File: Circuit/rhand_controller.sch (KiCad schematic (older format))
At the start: 17 parts, among them P7 BLUETOOTH, SW1 EmSW, SW2 SWITCH_INV, U1 STM32F042, U2 IM315TRX

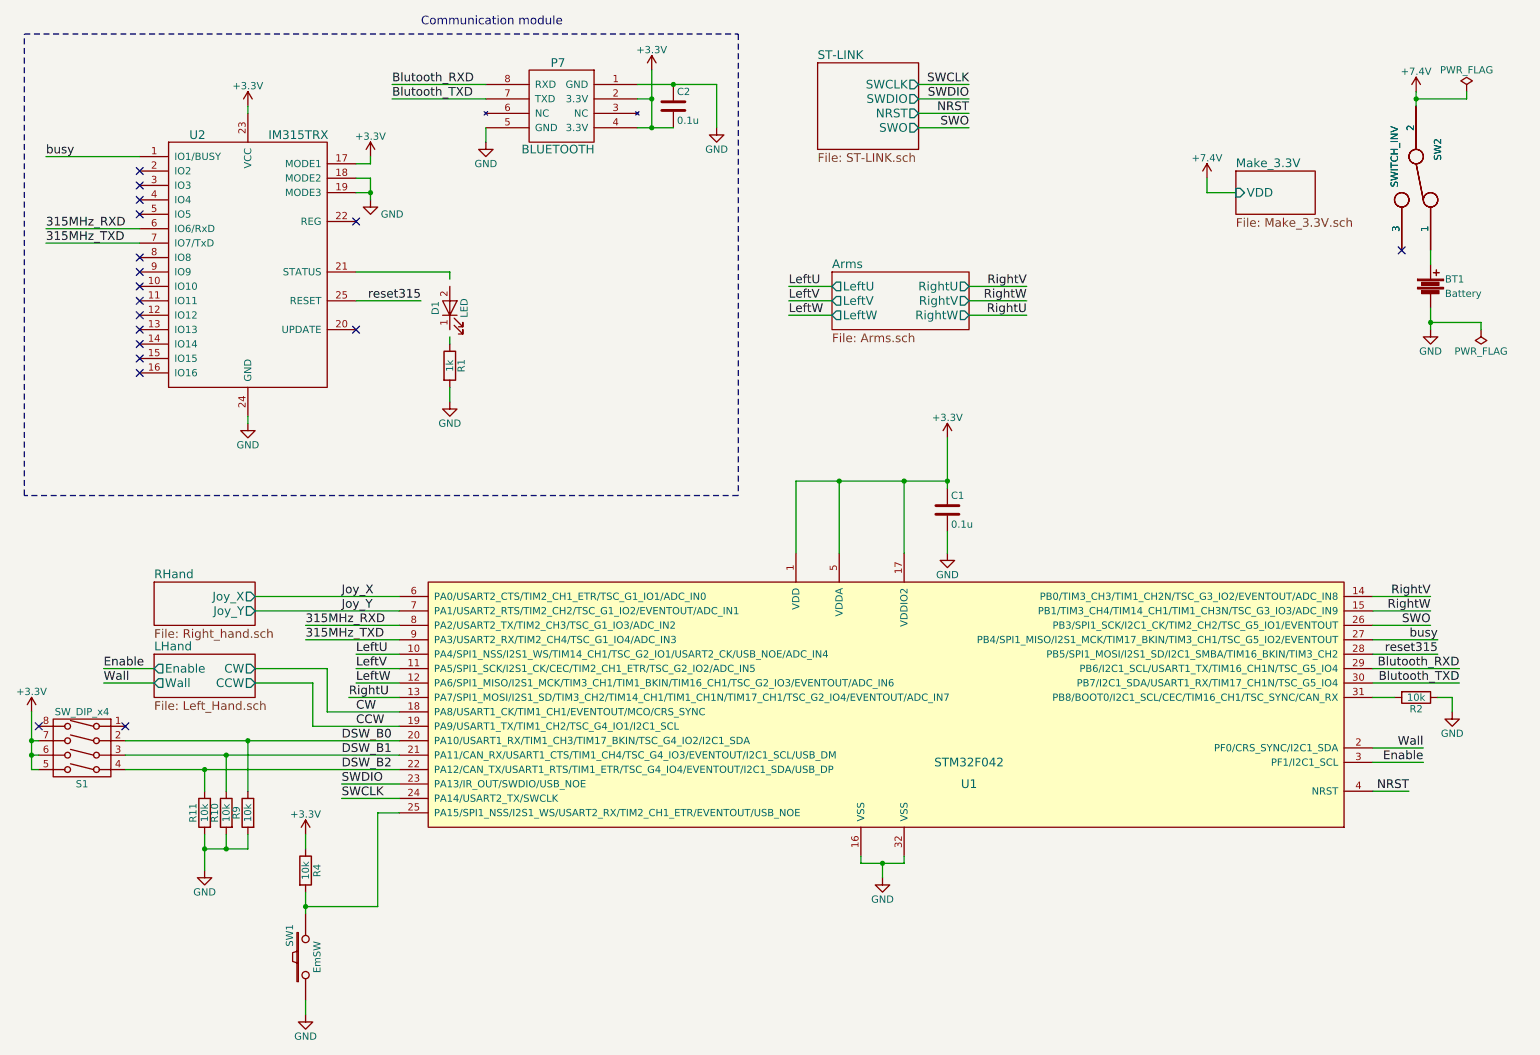
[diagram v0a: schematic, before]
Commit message: 部品割り付けの完了
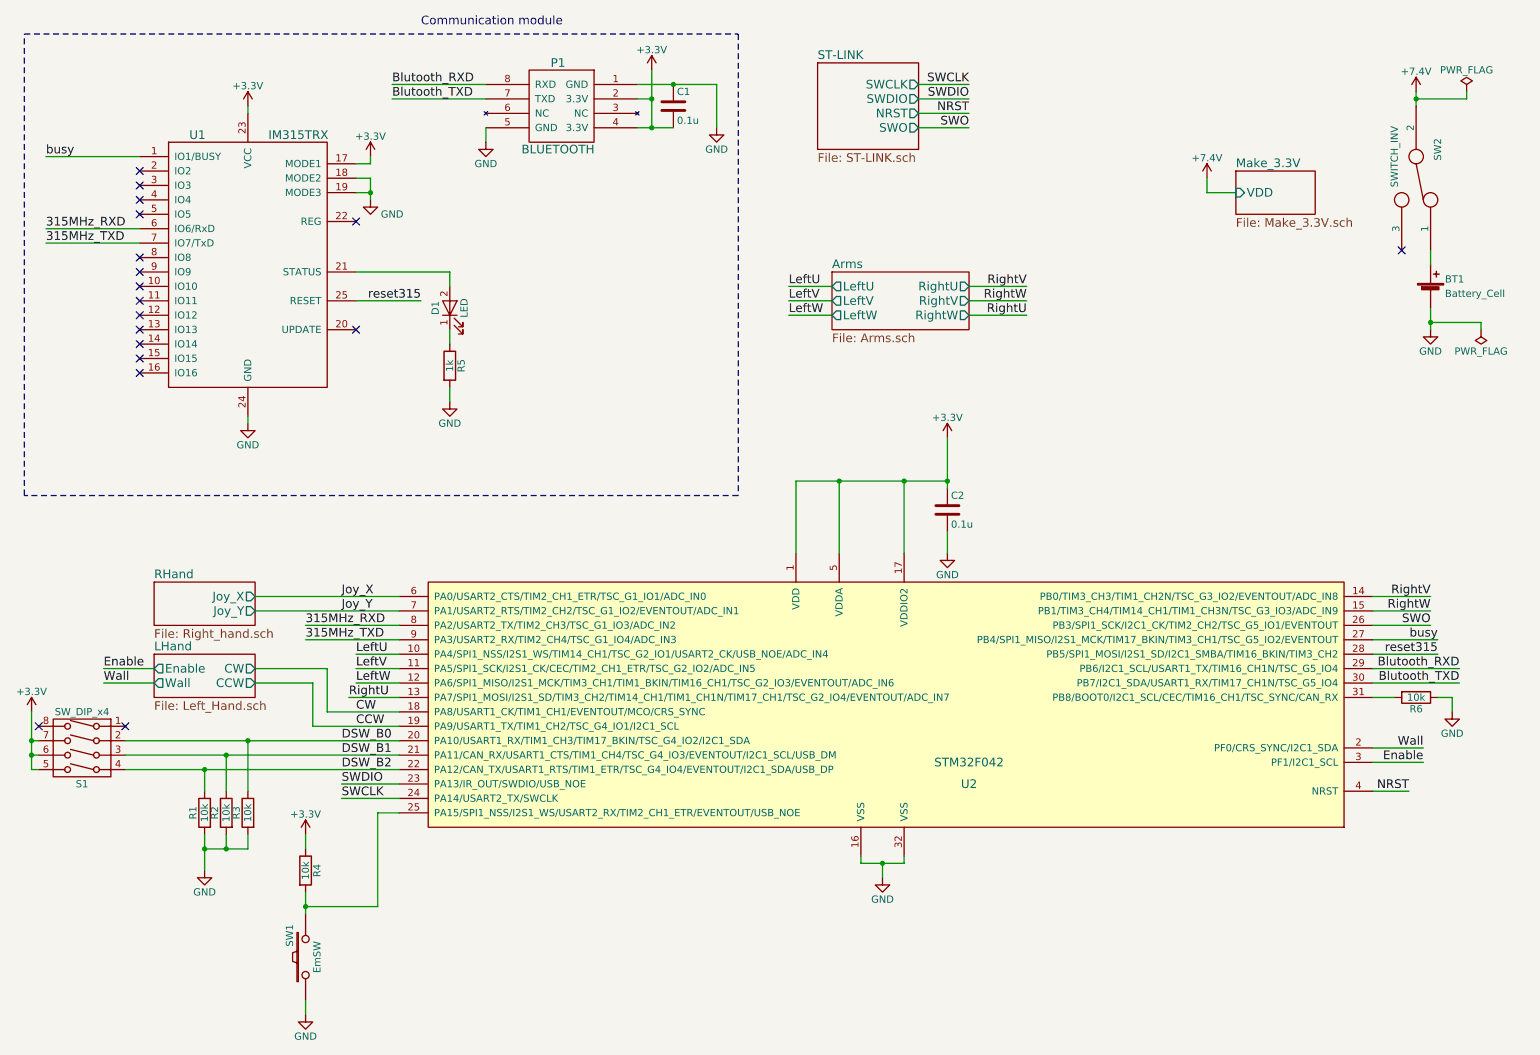
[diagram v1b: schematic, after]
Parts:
- removed BT1: Battery, YASU:XT_Mdot, symbol Battery
- removed SW2: SWITCH_INV, YASU:_SW_TGR, symbol SWITCH_INV
- added BT1: Battery_Cell, YASU:XT_Mdot, symbol Battery_Cell
- SW2: footprint (none) -> YASU:_SW_TGR
- renumbered C2 to C1, C1 to C2, P7 to P1, R11 to R1, R10 to R2, R9 to R3, R1 to R5, R2 to R6, U2 to U1, U1 to U2
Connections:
- net GND: now also BT1.2 (-)
- net at D1.1 (K): now also R5.1
- net at D1.2 (A): now also U1.21 (STATUS)
- net at SW2.1: now also BT1.1 (+)
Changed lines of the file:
@@
 LIBS:YASU
 LIBS:device
-LIBS:robocon_sch
 LIBS:rhand_controller-cache
 EELAYER 25 0
@@
 $EndSheet
 $Comp
-L STM32F042 U1
+L STM32F042 U2
 U 1 1 5936B864
 P 6600 5900
-F 0 "U1" H 7200 5800 60  0000 C CNN
+F 0 "U2" H 7200 5800 60  0000 C CNN
 F 1 "STM32F042" H 7200 5950 60  0000 C CNN
 F 2 "Housings_QFP:LQFP-32_7x7mm_Pitch0.8mm" H 7150 5800 60  0001 C CNN
@@
 $EndComp
 $Comp
-L BLUETOOTH P7
+L BLUETOOTH P1
 U 1 1 5936B91F
 P 4350 1400
-F 0 "P7" H 4350 1800 60  0000 C CNN
+F 0 "P1" H 4350 1800 60  0000 C CNN
 F 1 "BLUETOOTH" H 4350 1200 60  0000 C CNN
 F 2 "robocon_pcb:ESD200" H 4350 1400 60  0001 C CNN
@@
 $EndComp
 $Comp
-L C C1
+L C C2
 U 1 1 5936C50E
 P 7050 4100
-F 0 "C1" H 7075 4200 50  0000 L CNN
+F 0 "C2" H 7075 4200 50  0000 L CNN
 F 1 "0.1u" H 7075 4000 50  0000 L CNN
 F 2 "Capacitors_SMD:C_0805_HandSoldering" H 7088 3950 50  0001 C CNN
@@
 $EndComp
 $Comp
-L R R2
+L R R6
 U 1 1 5936E3FC
 P 10300 5400
-F 0 "R2" V 10380 5400 50  0000 C CNN
+F 0 "R6" V 10380 5400 50  0000 C CNN
 F 1 "10k" V 10300 5400 50  0000 C CNN
 F 2 "Resistors_SMD:R_0603_HandSoldering" V 10230 5400 50  0001 C CNN
@@
 DSW_B2
 $Comp
-L C C2
+L C C1
 U 1 1 5937C110
 P 5150 1300
-F 0 "C2" H 5175 1400 50  0000 L CNN
+F 0 "C1" H 5175 1400 50  0000 L CNN
 F 1 "0.1u" H 5175 1200 50  0000 L CNN
 F 2 "Capacitors_SMD:C_0805_HandSoldering" H 5188 1150 50  0001 C CNN
@@
 NoConn ~ 1450 2350
 $Comp
-L LED D1
-U 1 1 5938D7FB
-P 3600 2700
-F 0 "D1" H 3600 2800 50  0000 C CNN
-F 1 "LED" H 3600 2600 50  0000 C CNN
-F 2 "LEDs:LED_D5.0mm" H 3600 2700 50  0001 C CNN
-F 3 "" H 3600 2700 50  0001 C CNN
-	1    3600 2700
-	0    -1   -1   0
-$EndComp
-Wire Wire Line
-	2950 2450 3600 2450
-Wire Wire Line
-	3600 2450 3600 2500
-$Comp
-L R R1
+L R R5
 U 1 1 5938D995
 P 3600 3100
-F 0 "R1" V 3680 3100 50  0000 C CNN
+F 0 "R5" V 3680 3100 50  0000 C CNN
 F 1 "1k" V 3600 3100 50  0000 C CNN
 F 2 "Resistors_SMD:R_0603_HandSoldering" V 3530 3100 50  0001 C CNN
@@
 $EndComp
 $Comp
-L R R9
+L R R3
 U 1 1 593A8E23
 P 2200 6200
-F 0 "R9" V 2280 6200 50  0000 C CNN
+F 0 "R3" V 2280 6200 50  0000 C CNN
 F 1 "10k" V 2200 6200 50  0000 C CNN
 F 2 "Resistors_SMD:R_0603_HandSoldering" V 2130 6200 50  0001 C CNN
@@
 $EndComp
 $Comp
-L R R10
+L R R2
 U 1 1 593A8EB3
 P 2050 6200
-F 0 "R10" V 2130 6200 50  0000 C CNN
+F 0 "R2" V 2130 6200 50  0000 C CNN
 F 1 "10k" V 2050 6200 50  0000 C CNN
 F 2 "Resistors_SMD:R_0603_HandSoldering" V 1980 6200 50  0001 C CNN
@@
 $EndComp
 $Comp
-L R R11
+L R R1
 U 1 1 593A8F2B
 P 1900 6200
-F 0 "R11" V 1980 6200 50  0000 C CNN
+F 0 "R1" V 1980 6200 50  0000 C CNN
 F 1 "10k" V 1900 6200 50  0000 C CNN
 F 2 "Resistors_SMD:R_0603_HandSoldering" V 1830 6200 50  0001 C CNN
@@
 F 0 "SW2" H 10100 1950 50  0000 C CNN
 F 1 "SWITCH_INV" H 10150 1650 50  0000 C CNN
-F 2 "" H 10300 1800 50  0001 C CNN
+F 2 "YASU:_SW_TGR" H 10300 1800 50  0001 C CNN
 F 3 "" H 10300 1800 50  0000 C CNN
 	1    10300 1800
@@
 	10400 2300 10400 2400
 $Comp
-L IM315TRX U2
+L IM315TRX U1
 U 1 1 59414DD7
 P 2200 2400
-F 0 "U2" H 1850 3300 60  0000 C CNN
+F 0 "U1" H 1850 3300 60  0000 C CNN
 F 1 "IM315TRX" H 2550 3300 60  0000 C CNN
 F 2 "Pin_Headers:Pin_Header_Straight_2x13_Pitch1.27mm" H 1775 3175 60  0001 C CNN
@@
 NoConn ~ 1450 3150
 Wire Wire Line
-	3600 2900 3600 2950
-Wire Wire Line
 	3050 1900 2950 1900
 Connection ~ 3050 1900
@@
 NoConn ~ 2950 2850
 $Comp
-L Battery BT1
-U 1 1 594219DF
-P 10400 2550
-F 0 "BT1" H 10500 2600 50  0000 L CNN
-F 1 "Battery" H 10500 2500 50  0000 L CNN
-F 2 "YASU:XT_Mdot" V 10400 2590 50  0001 C CNN
-F 3 "" V 10400 2590 50  0000 C CNN
-	1    10400 2550
-	1    0    0    -1
-$EndComp
-$Comp
-L SWITCH_INV SW2
-U 1 1 5942A508
-P 10300 1800
-F 0 "SW2" H 10100 1950 50  0000 C CNN
-F 1 "SWITCH_INV" H 10150 1650 50  0000 C CNN
-F 2 "YASU:_SW_TGR" H 10300 1800 50  0001 C CNN
-F 3 "" H 10300 1800 50  0000 C CNN
-	1    10300 1800
-	0    1    1    0
+L Battery_Cell BT1
+U 1 1 59423E1E
+P 10400 2600
+F 0 "BT1" H 10500 2700 50  0000 L CNN
+F 1 "Battery_Cell" H 10500 2600 50  0000 L CNN
+F 2 "YASU:XT_Mdot" V 10400 2660 50  0001 C CNN
+F 3 "" V 10400 2660 50  0001 C CNN
+	1    10400 2600
+	1    0    0    -1
+$EndComp
+Wire Wire Line
+	3600 2950 3600 2850
+Wire Wire Line
+	2950 2450 3600 2450
+Wire Wire Line
+	3600 2450 3600 2550
+$Comp
+L LED D1
+U 1 1 59426E1D
+P 3600 2700
+F 0 "D1" H 3600 2800 50  0000 C CNN
+F 1 "LED" H 3600 2600 50  0000 C CNN
+F 2 "LEDs:LED_D5.0mm" H 3600 2700 50  0001 C CNN
+F 3 "" H 3600 2700 50  0001 C CNN
+	1    3600 2700
+	0    -1   -1   0
 $EndComp
 $EndSCHEMATC

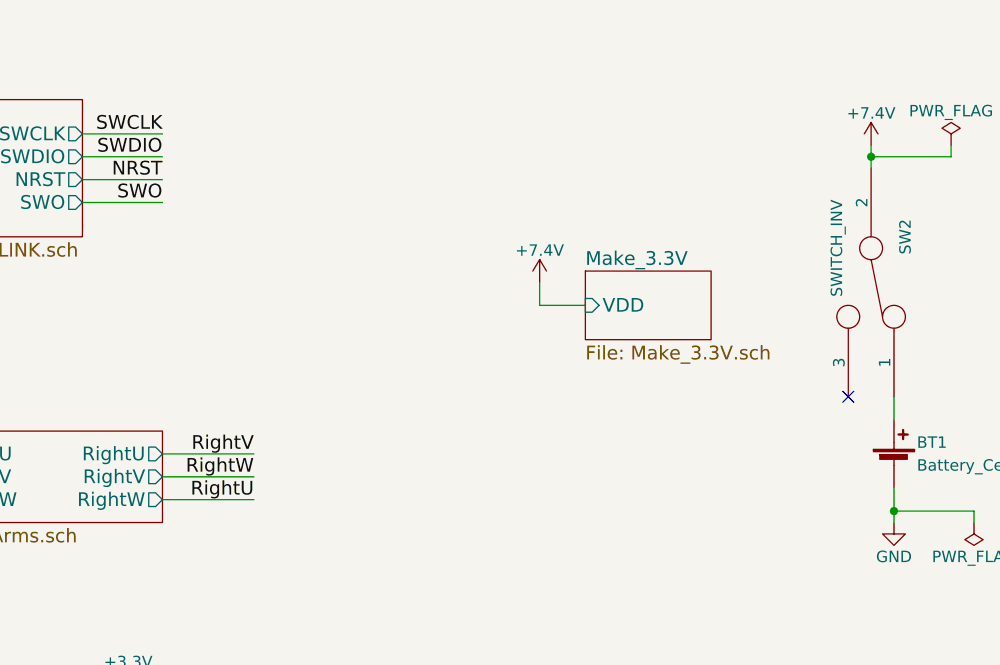
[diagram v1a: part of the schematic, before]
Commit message: 部品を基板上へ適当に配置
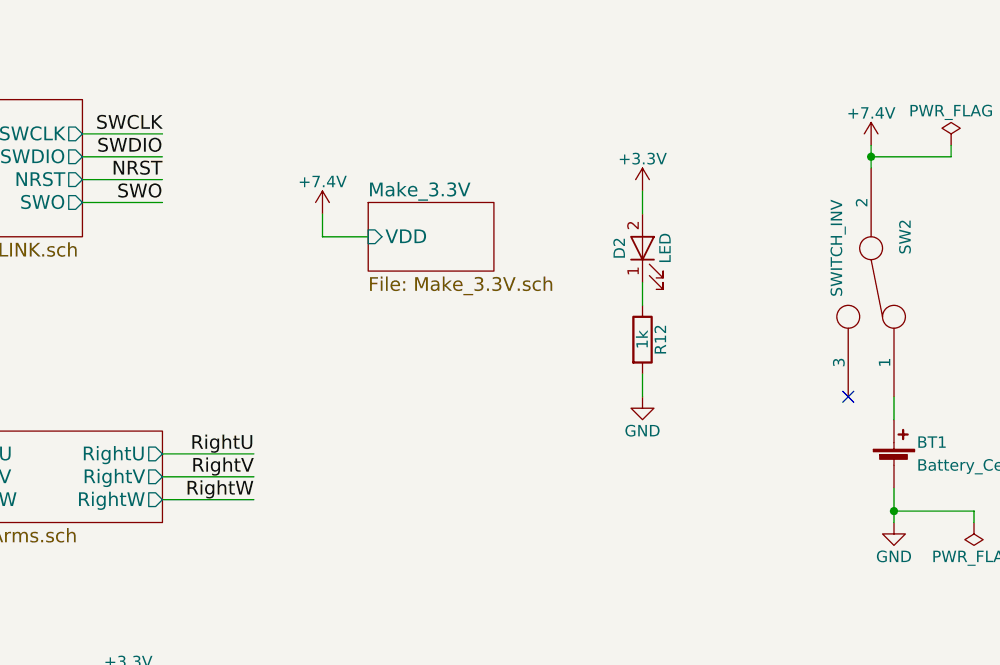
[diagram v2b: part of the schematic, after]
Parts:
- added D2: LED, LEDs:LED_D5.0mm, symbol LED
- added R12: 1k, Resistors_SMD:R_0603_HandSoldering, symbol R
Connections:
- net +3V3: now also D2.2 (A)
- net GND: now also R12.2
- new net: D2.1 (K), R12.1
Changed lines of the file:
@@
 $EndSheet
 $Sheet
-S 9050 1750 550  300
+S 8100 1450 550  300
 U 5936B5DF
 F0 "Make_3.3V" 60
 F1 "Make_3.3V.sch" 60
-F2 "VDD" I L 9050 1900 60
+F2 "VDD" I L 8100 1600 60
 $EndSheet
 $Comp
@@
 	3250 6100 2850 6100
 Wire Wire Line
-	9050 1900 8850 1900
-Wire Wire Line
-	8850 1900 8850 1800
+	8100 1600 7900 1600
+Wire Wire Line
+	7900 1600 7900 1500
 Wire Wire Line
 	10000 5200 10600 5200
@@
 L +7.4V #PWR012
 U 1 1 5938507B
-P 8850 1800
-F 0 "#PWR012" H 8850 1650 50  0001 C CNN
-F 1 "+7.4V" H 8850 1940 50  0000 C CNN
-F 2 "" H 8850 1800 50  0001 C CNN
-F 3 "" H 8850 1800 50  0001 C CNN
-	1    8850 1800
+P 7900 1500
+F 0 "#PWR012" H 7900 1350 50  0001 C CNN
+F 1 "+7.4V" H 7900 1640 50  0000 C CNN
+F 2 "" H 7900 1500 50  0001 C CNN
+F 3 "" H 7900 1500 50  0001 C CNN
+	1    7900 1500
 	1    0    0    -1
 $EndComp
@@
 Wire Wire Line
 	5950 2750 6250 2750
+Text Label 7600 2650 2    60   ~ 0
+RightV
+Text Label 7600 2750 2    60   ~ 0
+RightW
+Wire Wire Line
+	7200 2550 7600 2550
+Wire Wire Line
+	7200 2650 7600 2650
+Wire Wire Line
+	7600 2750 7200 2750
 Text Label 7600 2550 2    60   ~ 0
-RightV
-Text Label 7600 2650 2    60   ~ 0
-RightW
-Wire Wire Line
-	7200 2550 7600 2550
-Wire Wire Line
-	7200 2650 7600 2650
-Wire Wire Line
-	7600 2750 7200 2750
-Text Label 7600 2750 2    60   ~ 0
 RightU
 Wire Wire Line
@@
 	0    -1   -1   0
 $EndComp
+$Comp
+L LED D2
+U 1 1 59430038
+P 9300 1650
+F 0 "D2" H 9300 1750 50  0000 C CNN
+F 1 "LED" H 9300 1550 50  0000 C CNN
+F 2 "LEDs:LED_D5.0mm" H 9300 1650 50  0001 C CNN
+F 3 "" H 9300 1650 50  0001 C CNN
+	1    9300 1650
+	0    -1   -1   0
+$EndComp
+$Comp
+L R R12
+U 1 1 594300EF
+P 9300 2050
+F 0 "R12" V 9380 2050 50  0000 C CNN
+F 1 "1k" V 9300 2050 50  0000 C CNN
+F 2 "Resistors_SMD:R_0603_HandSoldering" V 9230 2050 50  0001 C CNN
+F 3 "" H 9300 2050 50  0001 C CNN
+	1    9300 2050
+	1    0    0    -1
+$EndComp
+$Comp
+L +3.3V #PWR022
+U 1 1 59430560
+P 9300 1400
+F 0 "#PWR022" H 9300 1250 50  0001 C CNN
+F 1 "+3.3V" H 9300 1540 50  0000 C CNN
+F 2 "" H 9300 1400 50  0001 C CNN
+F 3 "" H 9300 1400 50  0001 C CNN
+	1    9300 1400
+	1    0    0    -1
+$EndComp
+$Comp
+L GND #PWR023
+U 1 1 594310C6
+P 9300 2300
+F 0 "#PWR023" H 9300 2050 50  0001 C CNN
+F 1 "GND" H 9300 2150 50  0000 C CNN
+F 2 "" H 9300 2300 50  0001 C CNN
+F 3 "" H 9300 2300 50  0001 C CNN
+	1    9300 2300
+	1    0    0    -1
+$EndComp
+Wire Wire Line
+	9300 2300 9300 2200
+Wire Wire Line
+	9300 1900 9300 1800
+Wire Wire Line
+	9300 1500 9300 1400
 $EndSCHEMATC

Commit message: ピンヘッダを表面実装へ
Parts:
- U1: footprint Pin_Headers:Pin_Header_Straight_2x13_Pitch1.27mm -> Pin_Headers:Pin_Header_Straight_2x13_Pitch1.27mm_SMD
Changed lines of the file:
@@
 F 0 "U1" H 1850 3300 60  0000 C CNN
 F 1 "IM315TRX" H 2550 3300 60  0000 C CNN
-F 2 "Pin_Headers:Pin_Header_Straight_2x13_Pitch1.27mm" H 1775 3175 60  0001 C CNN
+F 2 "Pin_Headers:Pin_Header_Straight_2x13_Pitch1.27mm_SMD" H 1775 3175 60  0001 C CNN
 F 3 "" H 1775 3175 60  0001 C CNN
 	1    2200 2400

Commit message: あらかた終わったぞ
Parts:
- R12, R4: footprint Resistors_SMD:R_0603_HandSoldering -> Resistors_ThroughHole:R_Axial_DIN0207_L6.3mm_D2.5mm_P7.62mm_Horizontal
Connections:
- net 315MHz_RXD: now also U2.29 (PB6/I2C1_SCL/USART1_TX/TIM16_CH1N/TSC_G5_IO4); no longer U2.8 (PA2/USART2_TX/TIM2_CH3/TSC_G1_IO3/ADC_IN2)
- net 315MHz_TXD: now also U2.30 (PB7/I2C1_SDA/USART1_RX/TIM17_CH1N/TSC_G5_IO4); no longer U2.9 (PA3/USART2_RX/TIM2_CH4/TSC_G1_IO4/ADC_IN3)
- net Blutooth_RXD: now also U2.8 (PA2/USART2_TX/TIM2_CH3/TSC_G1_IO3/ADC_IN2); no longer U2.29 (PB6/I2C1_SCL/USART1_TX/TIM16_CH1N/TSC_G5_IO4)
- net Blutooth_TXD: now also U2.9 (PA3/USART2_RX/TIM2_CH4/TSC_G1_IO4/ADC_IN3); no longer U2.30 (PB7/I2C1_SDA/USART1_RX/TIM17_CH1N/TSC_G5_IO4)
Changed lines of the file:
@@
 Text Label 2850 6100 0    60   ~ 0
 SWCLK
-Text Label 10600 5300 2    60   ~ 0
+Text Label 2650 5000 0    60   ~ 0
 Blutooth_TXD
-Text Label 10600 5200 2    60   ~ 0
+Text Label 2650 4900 0    60   ~ 0
 Blutooth_RXD
 Text Label 3200 1150 0    60   ~ 0
@@
 	1    0    0    -1
 $EndComp
-Text Label 2600 4900 0    60   ~ 0
+Text Label 10650 5200 2    60   ~ 0
 315MHz_RXD
-Text Label 2600 5000 0    60   ~ 0
+Text Label 10650 5300 2    60   ~ 0
 315MHz_TXD
 Text Label 2850 5700 0    60   ~ 0
@@
 	7900 1600 7900 1500
 Wire Wire Line
-	10000 5200 10600 5200
-Wire Wire Line
-	10000 5300 10600 5300
+	3250 4900 2650 4900
+Wire Wire Line
+	3250 5000 2650 5000
 Wire Wire Line
 	3200 1150 3850 1150
@@
 	4900 1150 5450 1150
 Wire Wire Line
-	2600 4900 3250 4900
-Wire Wire Line
-	2600 5000 3250 5000
+	10650 5200 10000 5200
+Wire Wire Line
+	10650 5300 10000 5300
 Wire Wire Line
 	1350 5700 3250 5700
@@
 F 0 "R4" V 2680 6600 50  0000 C CNN
 F 1 "10k" V 2600 6600 50  0000 C CNN
-F 2 "Resistors_SMD:R_0603_HandSoldering" V 2530 6600 50  0001 C CNN
+F 2 "Resistors_ThroughHole:R_Axial_DIN0207_L6.3mm_D2.5mm_P7.62mm_Horizontal" V 2530 6600 50  0001 C CNN
 F 3 "" H 2600 6600 50  0000 C CNN
 	1    2600 6600
@@
 F 0 "R12" V 9380 2050 50  0000 C CNN
 F 1 "1k" V 9300 2050 50  0000 C CNN
-F 2 "Resistors_SMD:R_0603_HandSoldering" V 9230 2050 50  0001 C CNN
+F 2 "Resistors_ThroughHole:R_Axial_DIN0207_L6.3mm_D2.5mm_P7.62mm_Horizontal" V 9230 2050 50  0001 C CNN
 F 3 "" H 9300 2050 50  0001 C CNN
 	1    9300 2050
